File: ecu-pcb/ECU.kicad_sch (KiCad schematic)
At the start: 235 parts, among them J1 JTAG programming header, J3 USB-C receptacle, real Amphen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, J4 TE AMPSEAL 776180-1 (35-pos) 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, J5 TE AMPSEAL 776180-1 (35-pos) 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, J6 U.FL external BLE antenna con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, K1 Panasonic CB1a-T-P-12V automo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, Q1 SQM40020EL_GE3 automotive (AE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, Q10 FGP3040G2 automotive ignition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, Q11 PMV37ENEA automotive (AEC-Q10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, Q12 PMV37ENEA automotive (AEC-Q10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, Q13 PMV37ENEA automotive (AEC-Q10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, Q14 PMV37ENEA automotive (AEC-Q10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, Q15 PMV37ENEA automotive (AEC-Q10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, Q16 PMV37ENEA automotive (AEC-Q10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, Q17 PMV37ENEA automotive (AEC-Q10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, Q18 PMV37ENEA automotive (AEC-Q10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, Q2 PMV230ENEA automotive (AEC-Q1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, Q20 STD20NF06LAG automotive (AEC-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, Q21 STD20NF06LAG automotive (AEC-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, Q3 FGP3040G2 automotive ignition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, Q4 FGP3040G2 automotive ignition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, Q5 FGP3040G2 automotive ignition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, Q6 FGP3040G2 automotive ignition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, Q7 FGP3040G2 automotive ignition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, Q8 FGP3040G2 automotive ignition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, Q9 FGP3040G2 automotive ignition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, U1 NXP MPC5606B automotive (Qori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, U10 TLV2372-Q1 automotive (AEC-Q1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, U11 NXP TJA1043T automotive CAN t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, U12 NXP TJA1043T automotive CAN t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, U13 FTDI FT4232HA automotive (AEC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, U14 TI CC2640R2F-Q1 automotive BL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, U15 TI SN3257-Q1 automotive 4ch a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, U16 MAX9924 automotive (AEC-Q100)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, U17 TLV2372-Q1 automotive (AEC-Q1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, U18 Bosch CJ125 wideband O2 contr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, U19 ADS1118-Q1 EGT thermocouple A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, U2 LM74700-Q1 (AEC-Q100 G1), U20 NXP MC33926 ETC H-bridge (AEC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, U3 LMR33630-Q1 (AEC-Q100 G1), U4 TLV733P-Q1 (AEC-Q100 G1), U5 ST L9779WD-SPI automotive (Mu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, U6 ST L9779WD-SPI automotive (Mu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, U7 MAX9924 automotive (AEC-Q100)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, U8 MAX9924 automotive (AEC-Q100)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, U9 Bosch CJ125 wideband O2 contr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, Y1 8MHz (AEC-Q200), Y2 12MHz (AEC-Q200), Y3 24MHz (AEC-Q200)

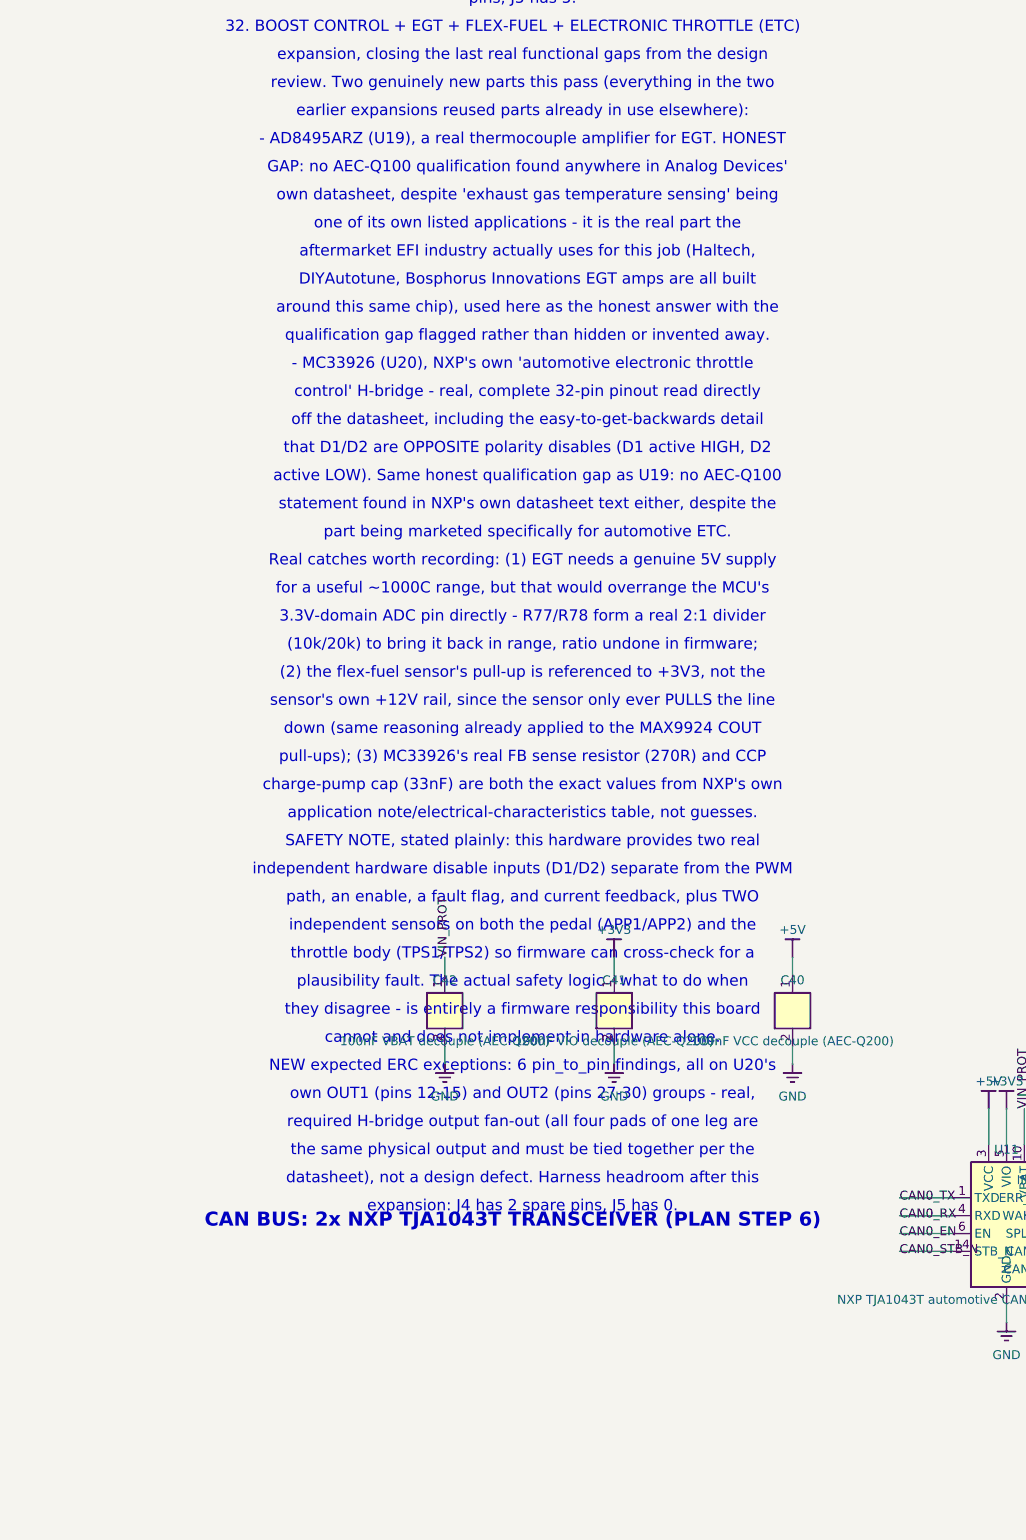
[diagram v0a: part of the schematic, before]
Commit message: Add board renders + generator; refresh stale on-sheet notes
render_white.py renders the current board (angled + top, transparent
composited onto white, same pattern as thermo-pcb) and now emits the
webp companions the site serves. Those were previously converted by
hand and had drifted: the pair sitting in the working tree still showed
the board from before the L9779 VDD5 regulator, the 40A relay, the
ADS1118-Q1 EGT front end and the balun. Generating them alongside the
PNGs removes the manual step that let them go stale.

The on-sheet NOTE_LINES still described U19 as an AD8495 with an
unresolved AEC-Q100 gap; updated to the ADS1118-Q1 that superseded it,
including why no thermocouple amplifier swap was possible.

Also excludes the fascia-pcb sibling project from this repo, matching
how manifold-pcb and thermo-pcb are already handled, and ignores the
ECU-erc.rpt that kicad-cli drops next to the schematic on every run.

Co-Authored-By: Claude Opus 5 <noreply@anthropic.com>
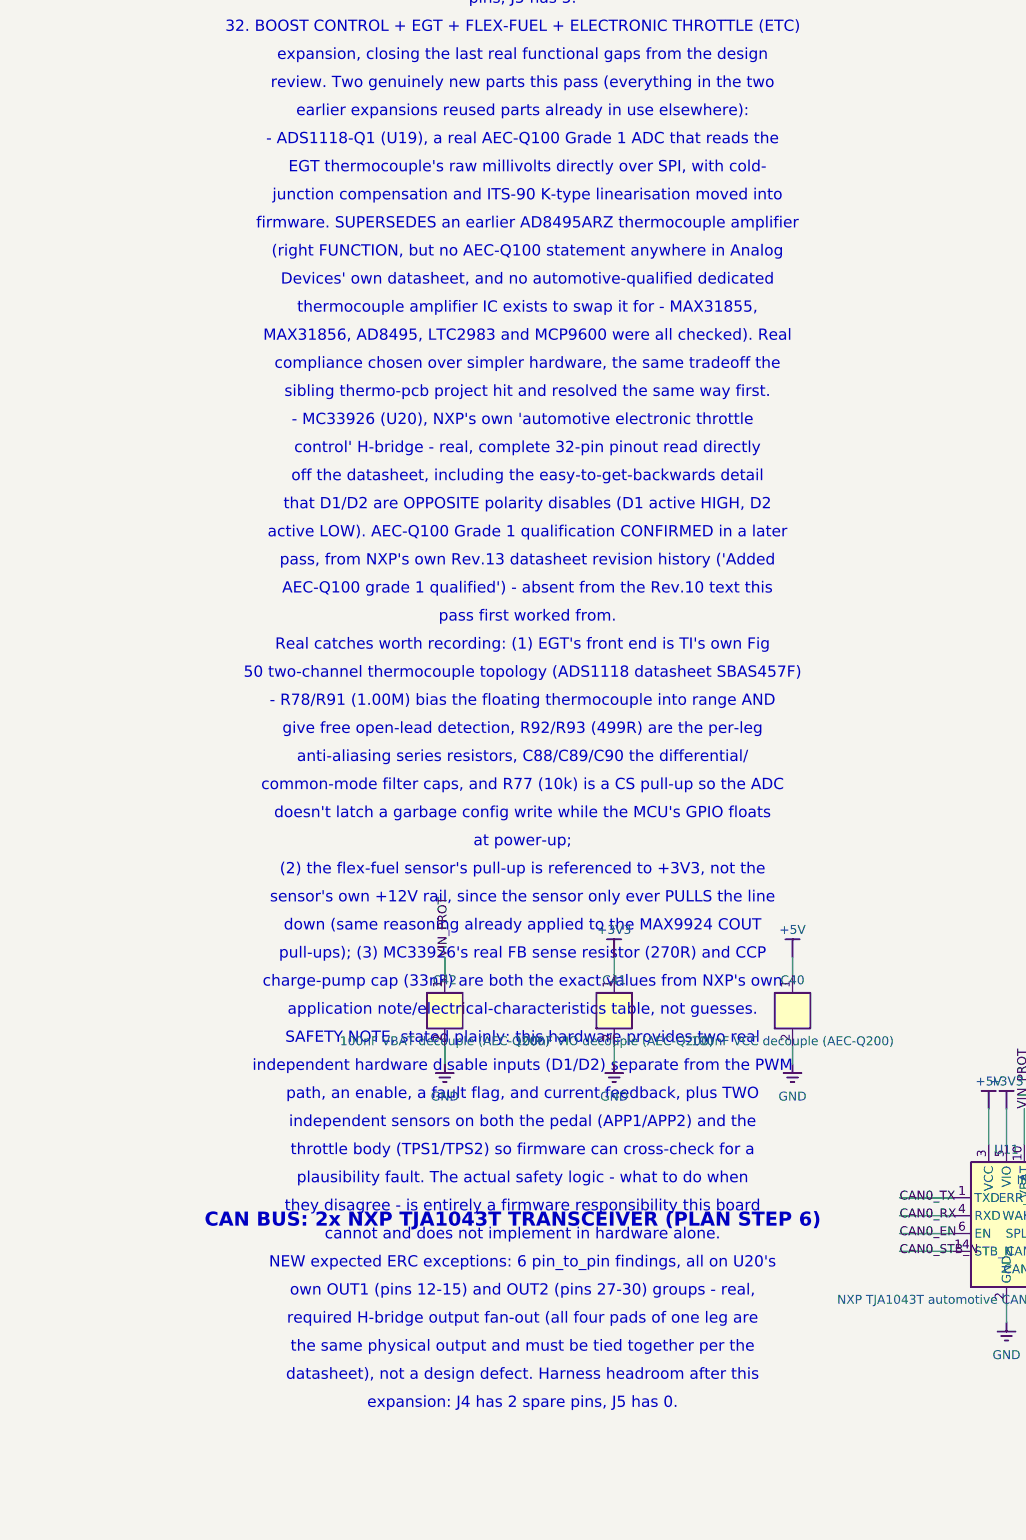
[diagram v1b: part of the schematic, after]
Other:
- note added: "(right FUNCTION, but no AEC-Q100 statement anywhere in Analog"
- note added: "- ADS1118-Q1 (U19), a real AEC-Q100 Grade 1 ADC that reads the"
- note added: "- R78/R91 (1.00M) bias the floating thermocouple into range AND"
- note added: "50 two-channel thermocouple topology (ADS1118 datasheet SBAS457F)"
- note added: "AEC-Q100 grade 1 qualified') - absent from the Rev.10 text this"
- note added: "Devices' own datasheet, and no automotive-qualified dedicated"
- note added: "EGT thermocouple's raw millivolts directly over SPI, with cold-"
- note added: "MAX31856, AD8495, LTC2983 and MCP9600 were all checked). Real"
- note added: "Real catches worth recording: (1) EGT's front end is TI's own Fig"
- note added: "active LOW). AEC-Q100 Grade 1 qualification CONFIRMED in a later"
- note added: "anti-aliasing series resistors, C88/C89/C90 the differential/"
- note added: "at power-up;"
- note added: "common-mode filter caps, and R77 (10k) is a CS pull-up so the ADC"
- note added: "compliance chosen over simpler hardware, the same tradeoff the"
- note added: "doesn't latch a garbage config write while the MCU's GPIO floats"
- note added: "firmware. SUPERSEDES an earlier AD8495ARZ thermocouple amplifier"
- note added: "give free open-lead detection, R92/R93 (499R) are the per-leg"
- note added: "junction compensation and ITS-90 K-type linearisation moved into"
- note added: "pass first worked from."
- note added: "pass, from NXP's own Rev.13 datasheet revision history ('Added"
- note added: "sibling thermo-pcb project hit and resolved the same way first."
- note added: "thermocouple amplifier IC exists to swap it for - MAX31855,"
- note removed: "(10k/20k) to bring it back in range, ratio undone in firmware;"
- note removed: "- AD8495ARZ (U19), a real thermocouple amplifier for EGT. HONEST"
- note removed: "3.3V-domain ADC pin directly - R77/R78 form a real 2:1 divider"
- note removed: "DIYAutotune, Bosphorus Innovations EGT amps are all built"
- note removed: "GAP: no AEC-Q100 qualification found anywhere in Analog Devices'"
- note removed: "Real catches worth recording: (1) EGT needs a genuine 5V supply"
- note removed: "active LOW). Same honest qualification gap as U19: no AEC-Q100"
- note removed: "aftermarket EFI industry actually uses for this job (Haltech,"
- note removed: "around this same chip), used here as the honest answer with the"
- note removed: "for a useful ~1000C range, but that would overrange the MCU's"
- note removed: "one of its own listed applications - it is the real part the"
- note removed: "own datasheet, despite 'exhaust gas temperature sensing' being"
- note removed: "part being marketed specifically for automotive ETC."
- note removed: "qualification gap flagged rather than hidden or invented away."
- note removed: "statement found in NXP's own datasheet text either, despite the"

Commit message: Divide the eight 5V sensor inputs down to the 3.3V ADC
MAP, TPS, APP1, APP2, TPS1, TPS2, OILP and FUELP are all external 5V
ratiometric sensors, but this MCU's ADC reference is VDD_HV_ADC0/1 at
3.3V, and each of those eight had only a 1k + 22nF RC filter in front of
it -- no divider. Everything above 3.3V converted to 0xFFF, so a
10-105 kPa MAP sensor stopped reading at ~73 kPa: the ECU went blind
from part throttle upward, exactly where a fuelling error damages
pistons. It also defeated the APP1/APP2 and TPS1/TPS2 redundancy
comparison the ETC hardware exists for -- two channels that both clamp
at full scale agree with each other perfectly while both being wrong.

An oversight rather than a choice: the board divides correctly
everywhere else (VBATT 68k/10k, IAT/CLT pulled up to 3.3V not 5V).

NOT a device-damage bug, which is worth stating because it changes the
urgency. Table 42 footnote 3 of the MPC5606BK data sheet says VAINx may
exceed VDD_ADC1 while remaining within absolute maximum ratings, with
the conversion simply clamping, and the 1k series resistors held pad
injection to ~1.4mA against the +/-5mA IINJ limit. A measurement
failure, not a smoke failure.

4.7k/4.7k 1% was derived, not picked. Table 42 footnote 4 gives no fixed
source-impedance limit -- it requires the source to charge CS within
tADC1_S -- so it was solved from the real numbers. Worst case IGNORING
the 22nF cap: 1/2 LSB at 12 bits is ln(2*4096) = 9.01 time constants
inside the 500ns Tsample floor the Reference Manual states as a hardware
requirement (Table 28-1 fn 3), against CS 5pF + CP1/2/3 5.5pF = 10.5pF
and internal RSW2 2k + RAD 0.3k. That allows 5.29k total, so 2.99k
external; the chosen Thevenin 2.35k fits with margin. With the cap
fitted it is looser still: a ~2000:1 charge reservoir, so charge sharing
costs 0.048% as a systematic gain error (~1.5 LSB against +/-6 LSB TUE)
and recovers with tau = 52us against millisecond sample intervals.
Higher values would load the sensor less but 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
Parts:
- added R100: 4.7k 1% TPS1 divider lo (AEC-Q200), Resistor_SMD:R_0603_1608Metric, symbol ECU:R_V
- added R101: 4.7k 1% TPS2 divider lo (AEC-Q200), Resistor_SMD:R_0603_1608Metric, symbol ECU:R_V
- added R94: 4.7k 1% MAP divider lo (AEC-Q200), Resistor_SMD:R_0603_1608Metric, symbol ECU:R_V
- added R95: 4.7k 1% TPS divider lo (AEC-Q200), Resistor_SMD:R_0603_1608Metric, symbol ECU:R_V
- added R96: 4.7k 1% oil-pressure divider lo (AEC-Q200), Resistor_SMD:R_0603_1608Metric, symbol ECU:R_V
- added R97: 4.7k 1% fuel-pressure divider lo (AEC-Q200), Resistor_SMD:R_0603_1608Metric, symbol ECU:R_V
- added R98: 4.7k 1% APP1 divider lo (AEC-Q200), Resistor_SMD:R_0603_1608Metric, symbol ECU:R_V
- added R99: 4.7k 1% APP2 divider lo (AEC-Q200), Resistor_SMD:R_0603_1608Metric, symbol ECU:R_V
- R22: value 1k MAP RC filter (AEC-Q200) -> 4.7k 1% MAP divider hi (AEC-Q200)
- R23: value 1k TPS RC filter (AEC-Q200) -> 4.7k 1% TPS divider hi (AEC-Q200)
- R25: value 1.00k CLT pull-up (AEC-Q200) - real GM-style sending unit, same sizing as thermo-pcb's R12 -> 1k 1% CLT pull-up (AEC-Q200) - real GM-style sending unit, same sizing as thermo-pcb's R12
- R46: value 4k7 US series R to UP node (AEC-Q200) - real Bosch -> 4.7k US series R to UP node (AEC-Q200) - real Bosch
- R53: value 1k oil-pressure RC filter (AEC-Q200) -> 4.7k 1% oil-pressure divider hi (AEC-Q200)
- R54: value 1k fuel-pressure RC filter (AEC-Q200) -> 4.7k 1% fuel-pressure divider hi (AEC-Q200)
- R73: value 4k7 US series R to UP node (AEC-Q200) -> 4.7k US series R to UP node (AEC-Q200)
- R78: value 1.00M EGT TC bias pull-up (AEC-Q200) - real TI Fig 50 value -> 1M EGT TC bias pull-up (AEC-Q200) - real TI Fig 50 value
- R80: value 4k7 flex-fuel pull-up to +3V3 (AEC-Q200) -> 4.7k flex-fuel pull-up to +3V3 (AEC-Q200)
- R87: value 1k APP1 RC filter (AEC-Q200) -> 4.7k 1% APP1 divider hi (AEC-Q200)
- R88: value 1k APP2 RC filter (AEC-Q200) -> 4.7k 1% APP2 divider hi (AEC-Q200)
- R89: value 1k TPS1 RC filter (AEC-Q200) -> 4.7k 1% TPS1 divider hi (AEC-Q200)
- R90: value 1k TPS2 RC filter (AEC-Q200) -> 4.7k 1% TPS2 divider hi (AEC-Q200)
- R91: value 1.00M EGT TC bias pull-down (AEC-Q200) - real TI Fig 50 value -> 1M EGT TC bias pull-down (AEC-Q200) - real TI Fig 50 value
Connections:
- net APP1_ADC: now also R98.1
- net APP2_ADC: now also R99.1
- net FUELP_ADC: now also R97.1
- net GND: now also R100.2, R101.2, R94.2, R95.2, R96.2, R97.2, R98.2, R99.2
- net MAP_ADC: now also R94.1
- net OILP_ADC: now also R96.1
- net TPS1_ADC: now also R100.1
- net TPS2_ADC: now also R101.1
- net TPS_ADC: now also R95.1
